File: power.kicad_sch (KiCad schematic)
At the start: 105 parts, among them J3 353180620, J4 353180620, J5 353180620, U5 AP3211, U6 TPS53667RTAR

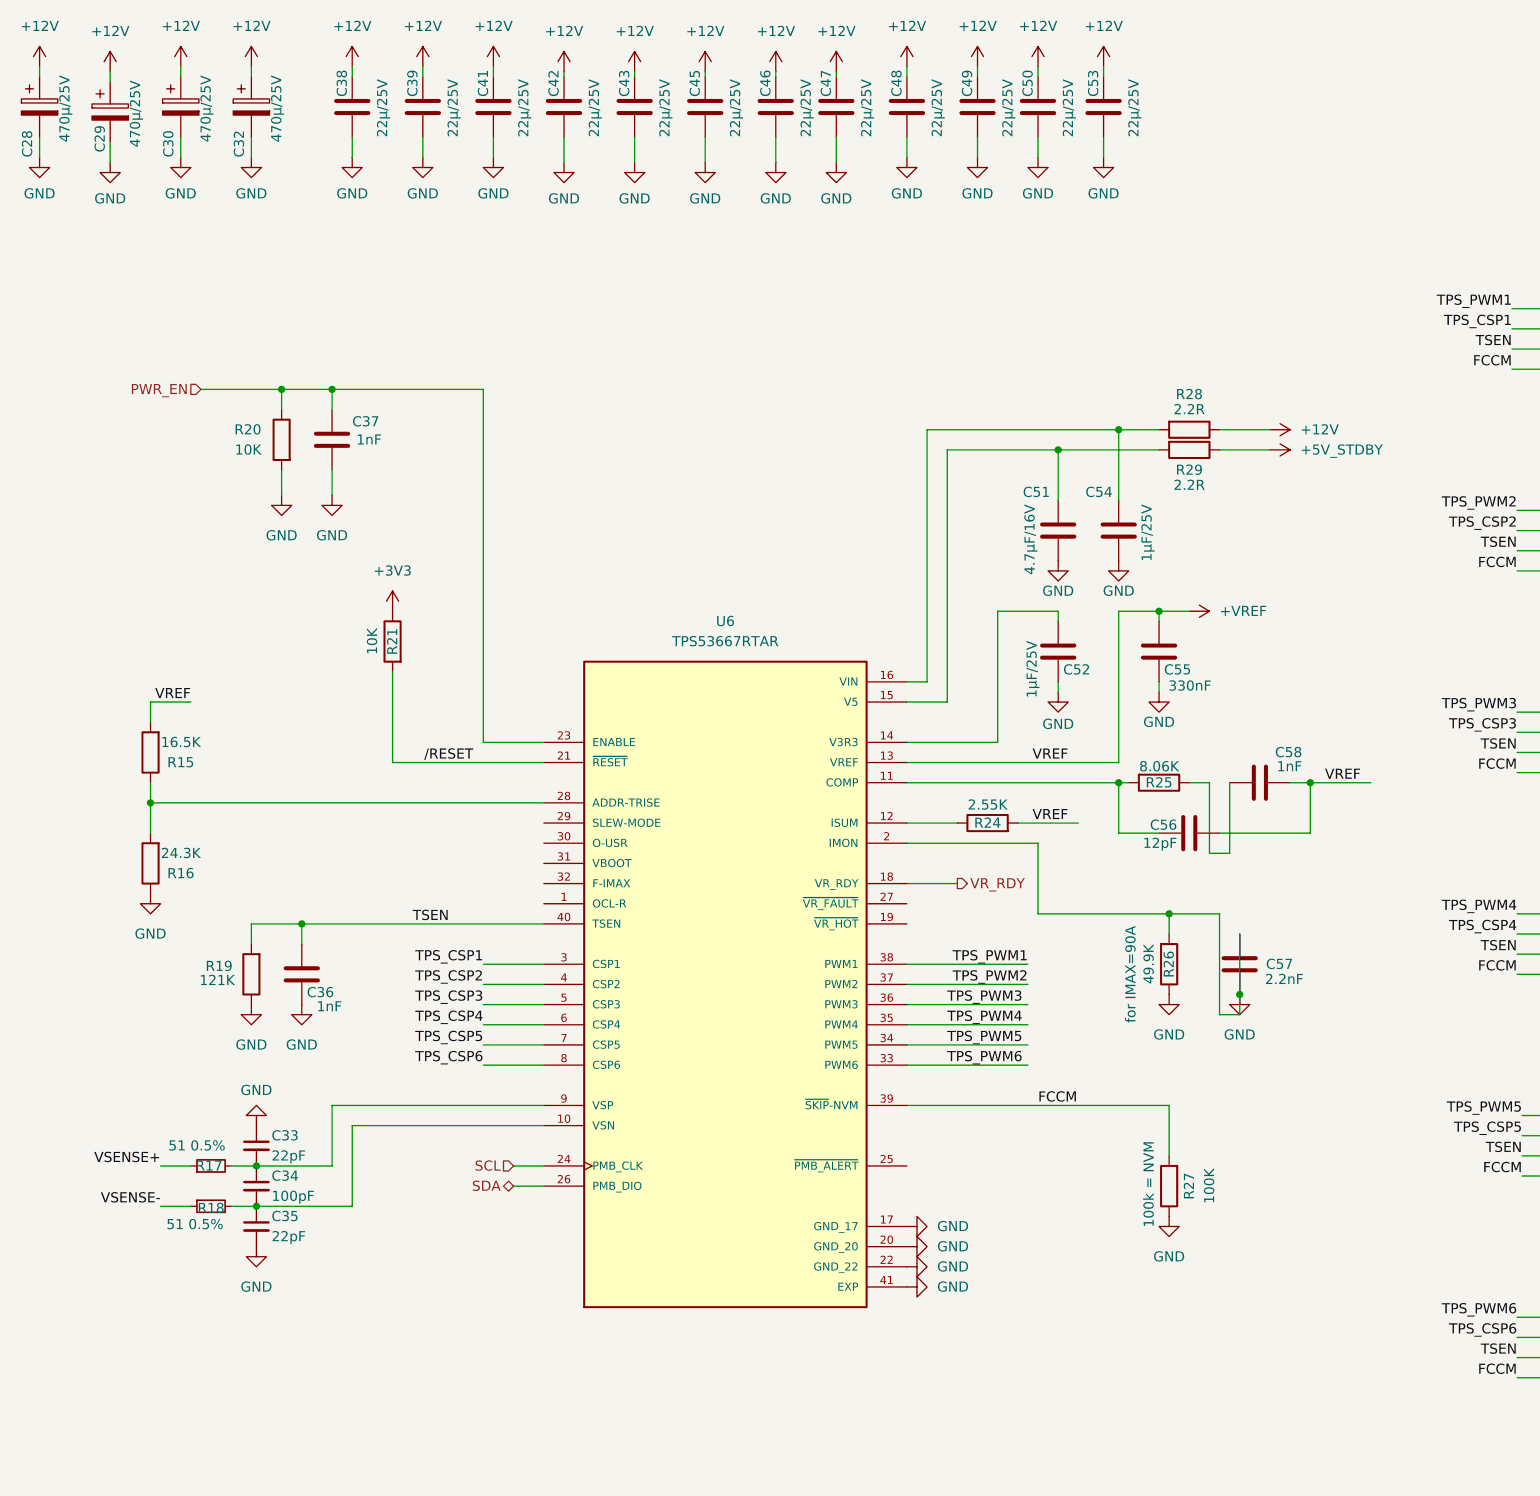
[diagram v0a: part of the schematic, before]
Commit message: board stakup updated and schematic is updated
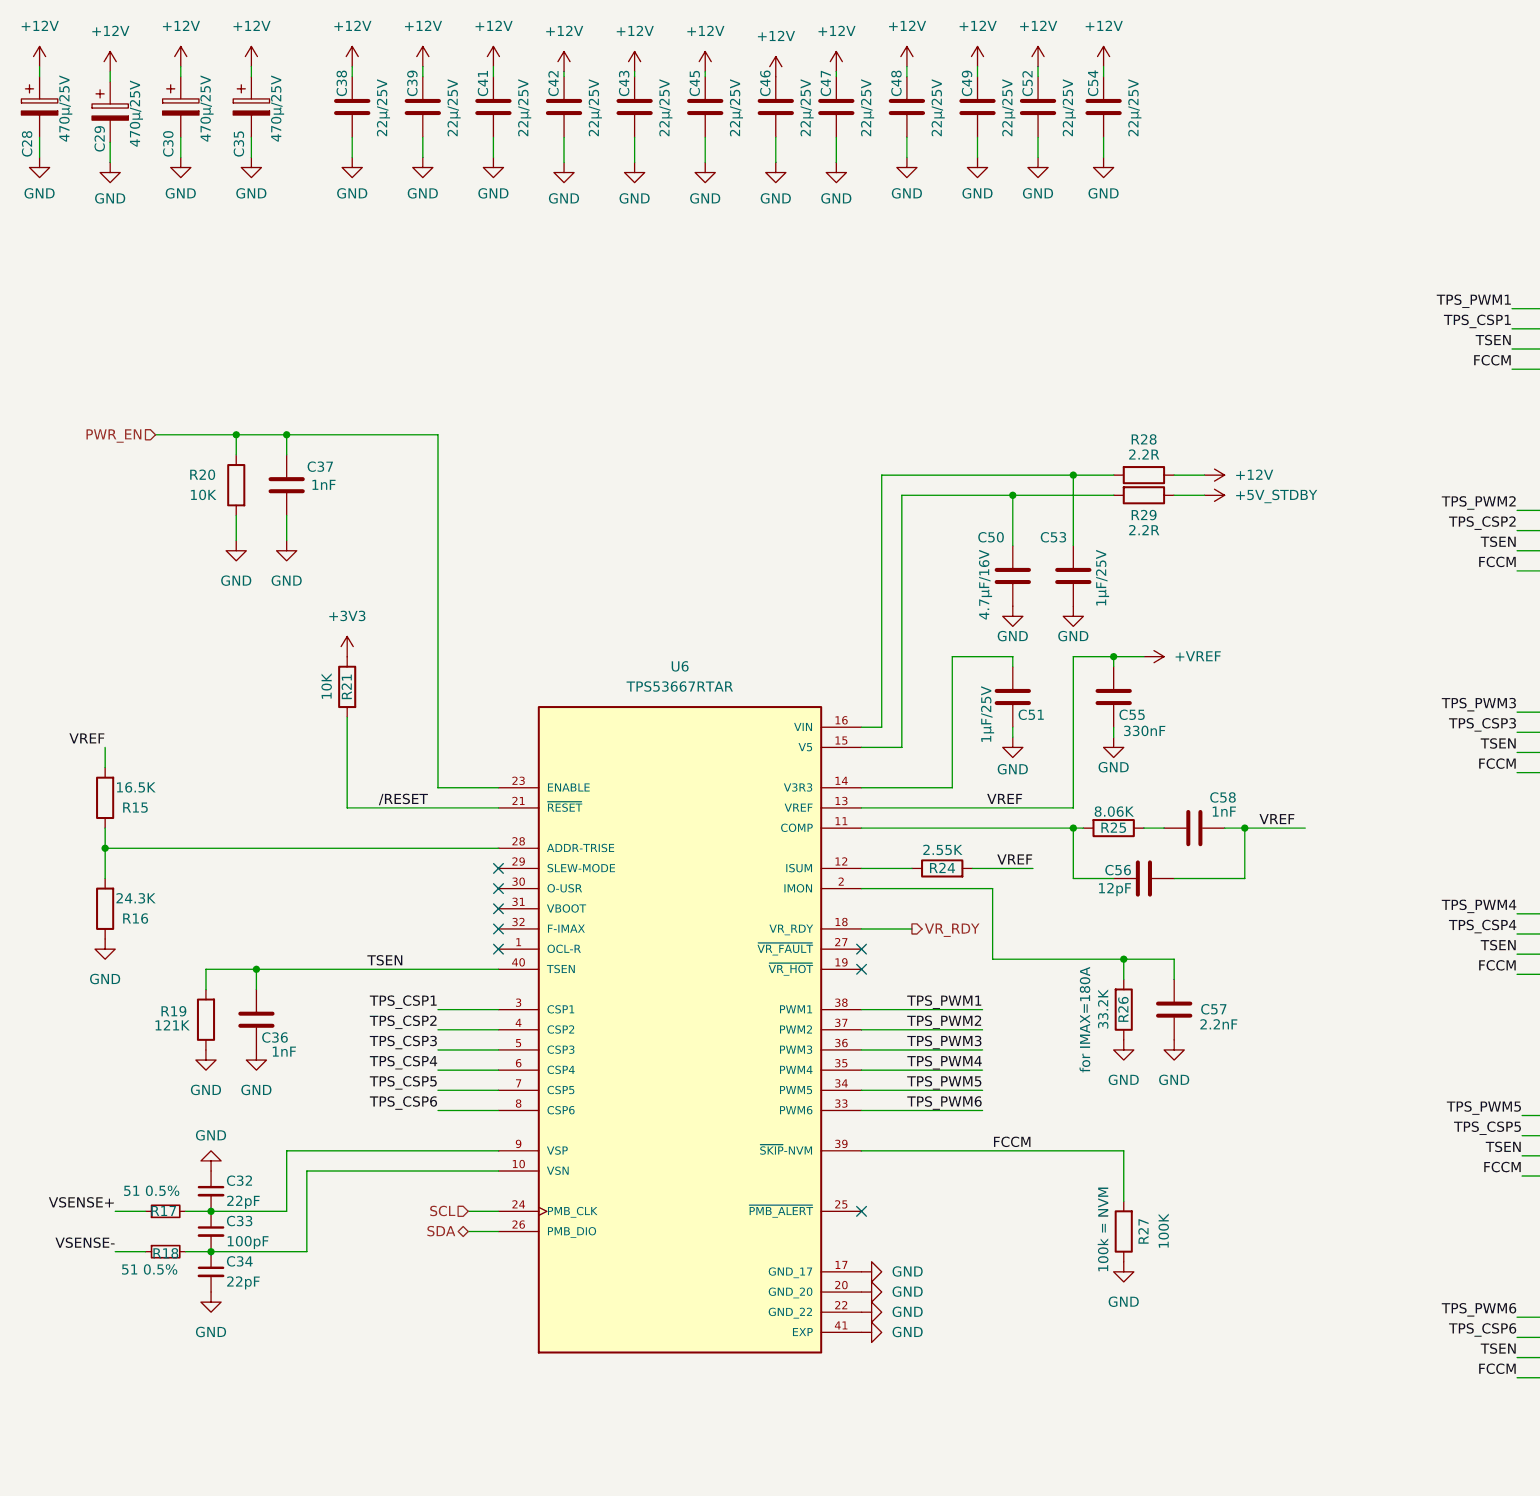
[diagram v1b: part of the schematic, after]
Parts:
- removed C35: 22pF, Capacitor_SMD:C_0805_2012Metric, symbol Device:C_Small
- removed C52, C54: 1µF/25V, Capacitor_SMD:C_0805_2012Metric, symbol Device:C
- added C32: 22pF, Capacitor_SMD:C_0805_2012Metric, symbol Device:C_Small
- added C50: 4.7µF/16V, Capacitor_SMD:C_0805_2012Metric, symbol Device:C
- added C53: 1µF/25V, Capacitor_SMD:C_0805_2012Metric, symbol Device:C
- C33: value 22pF -> 100pF; Manufacturer CL21C220JBANNNC -> 0805B101M250CT; P/N LCSC (none) -> C3897824; P/N MOUSER 187-CL21C220JBANNNC -> 791-0805B101M250CT
- C34: value 100pF -> 22pF; Manufacturer 0805B101M250CT -> CL21C220JBANNNC; P/N LCSC (none) -> C1804; P/N MOUSER 791-0805B101M250CT -> 187-CL21C220JBANNNC
- C36, C37, C58: P/N LCSC (none) -> C106244
- C51: value 4.7µF/16V -> 1µF/25V; Manufacturer CL21A475KOFNNNG -> CL21B105KAFNNNE; P/N LCSC (none) -> C344171; P/N MOUSER 187-CL21A475KOFNNNG -> 187-CL21B105KAFNNNE
- C55: P/N LCSC (none) -> C73142
- C56: P/N LCSC (none) -> C20218205
- C57: P/N LCSC (none) -> C3907092
- R15: P/N LCSC (none) -> C35929
- R16: P/N LCSC (none) -> C17569
- R17, R18: P/N LCSC (none) -> C868849
- R19: P/N LCSC (none) -> C17438
- R20, R21: P/N LCSC (none) -> C84376
- R24: P/N LCSC (none) -> C2933383
- R25: P/N LCSC (none) -> C2933501
- R26: value 49.9K -> 33.2K; Manufacturer CR0805-FX-4992ELF -> RMCF0805FT33K2; P/N LCSC (none) -> C3016779; P/N MOUSER 652-CR0805FX-4992ELF -> 708-RMCF0805FT33K2
- R27: P/N LCSC (none) -> C149504
- R28, R29: P/N LCSC (none) -> C17521
- U6: footprint TPS53667RTAR:IC_TPS53667RTAR -> EKO_Miner_ASIClib:TPS53667RTAR; P/N LCSC (none) -> C702270
- renumbered C32 to C35, C50 to C52, C53 to C54
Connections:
- net GND: now also C34.2, C51.2, C32.1, C50.1, C53.1; no longer C33.1, C51.1, C57.1, R26.2, U6.2 (IMON)
- net at R18.2, U6.10 (VSN): now also C33.2, C34.1; no longer C34.2
- net at U6.14 (V3R3): now also C51.1
- net at R29.2, U6.15 (V5): now also C50.2; no longer C51.2
- net at R28.2, U6.16 (VIN): now also C53.2
- net at R17.2, U6.9 (VSP): now also C33.1, C32.2; no longer C33.2, C34.1
- new net: C57.1, R26.2, U6.2 (IMON)
- no-connect marks 0 -> 8
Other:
- note added: "for IMAX=180A"
- note removed: "for IMAX=90A"

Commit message: updated schematic working on layout
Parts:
- U6: footprint EKO_Miner_ASIClib:TPS53667RTAR -> TPS53667RTAR:IC_TPS53667RTAR
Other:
- company: (none) -> Author: Aadhi M
- title: (none) -> PC-AXE
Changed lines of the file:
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@@
 	(generator_version "9.0")
 	(paper "A3")
+	(title_block
+		(title "PC-AXE")
+		(company "Author: Aadhi M")
+	)
 	(text "100k = NVM"
 		(exclude_from_sim no)
@@
 			)
 		)
-		(property "Footprint" "EKO_Miner_ASIClib:TPS53667RTAR"
+		(property "Footprint" "TPS53667RTAR:IC_TPS53667RTAR"
 			(at 98.425 140.335 0)
 			(effects
@@
 			(project "PC-AXE"
 				(path "/540dc3bd-590a-41f0-90cd-0aeeeb4ef5ba/049cc3a6-36b5-4dee-bdf2-7e5f4e5480ae"
-					(page "7")
+					(page "5")
 				)
 			)

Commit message: Updated new layout and routing of PCB
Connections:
- net +12V: now also J3.1, J3.2, J3.3, J4.1, J4.2, J4.3, J5.1, J5.2, J5.3; no longer J3.4, J3.5, J3.6, J4.4, J4.5, J4.6, J5.4, J5.5, J5.6
- net GND: now also J3.4, J3.5, J3.6, J4.4, J4.5, J4.6, J5.4, J5.5, J5.6; no longer J3.1, J3.2, J3.3, J4.1, J4.2, J4.3, J5.1, J5.2, J5.3
